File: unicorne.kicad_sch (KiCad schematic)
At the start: 22 parts, among them J1 Battery, J2 TPS43, J3 Expansion, J4 GPIO, J5 PAW3395 / PMW3360, J6 LED power in, Q1 AO3401A, Q2 2N7002, SW43 Power, SW44 Reset, U1 nice!nano v2, U2 SN74LV1T125

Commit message: 0603 resistors and capacitors; rerouted; router rescues stuck signals
- R1-R5, C1, C2 move to KiCad's 0603 hand-solder footprints (README and the
  layout page updated). The last 0805 version is tagged working_0805.
- finish_route.py: when every attempt leaves a signal unrouted, lift one
  neighbouring net in the way, route the connection, reroute the lifted net,
  and keep it only if nothing new is left unrouted. Tracks are removed by
  editing the board file, since removing them through the bindings breaks
  them.
- Both boards: DRC 0 unconnected, schematic parity 0, every pin, the matrix,
  the LED chain and one GND group verified. Gerbers, STEP, renders and plates
  regenerated.

Co-Authored-By: Claude Opus 5.5 <noreply@anthropic.com>
Claude-Session: https://claude.ai/code/session_01D39ubfTYtq6FMvNmmbStTo
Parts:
- C1, C2: footprint Capacitor_SMD:C_0805_2012Metric_Pad1.18x1.45mm_HandSolder -> Capacitor_SMD:C_0603_1608Metric_Pad1.08x0.95mm_HandSolder
- R1, R2, R3, R4, R5: footprint Resistor_SMD:R_0805_2012Metric_Pad1.20x1.40mm_HandSolder -> Resistor_SMD:R_0603_1608Metric_Pad0.98x0.95mm_HandSolder

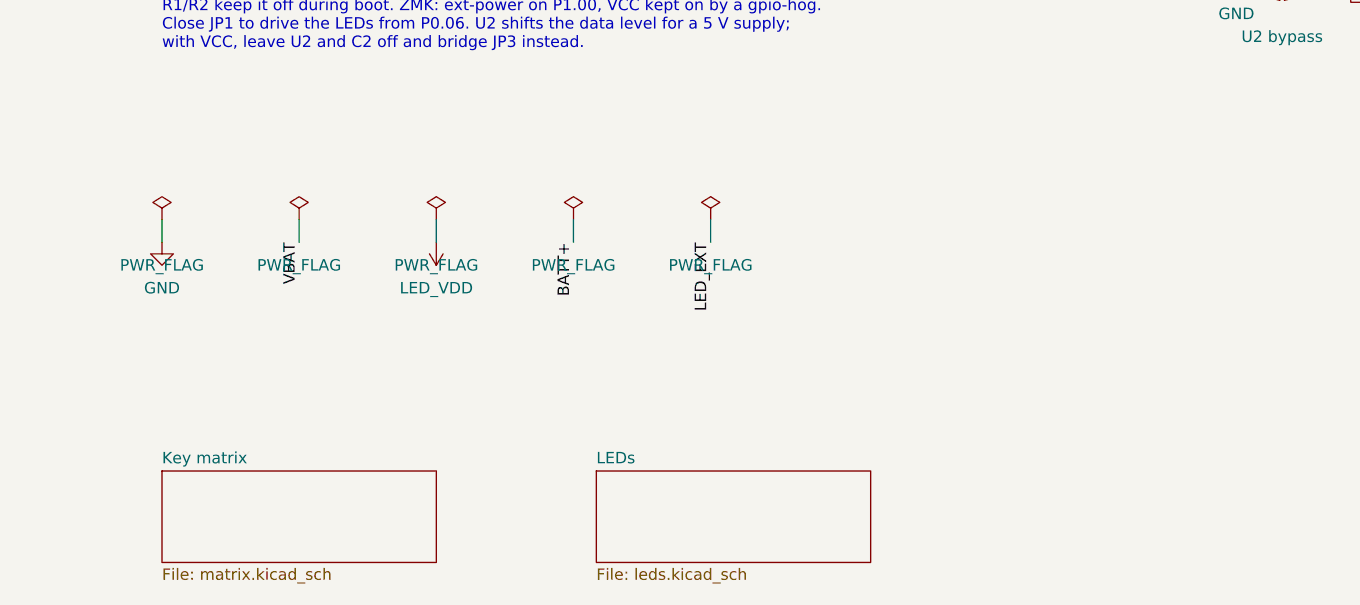
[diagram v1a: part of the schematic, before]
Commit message: Unrouted boards: Pro Micro jumpers, hand-placed centre, new pad rows
Pro Micro mode jumpers JP4-JP6, the hand placement (LED cluster at the
bottom, battery pads by the power switch, reset beside the nice!nano), the
sensor/pull-up/trackpad/UART rows below the nice!nano, and silkscreen that
follows every part. No tracks, vias or zones.

Co-Authored-By: Claude Opus 5.5 <noreply@anthropic.com>
Claude-Session: https://claude.ai/code/session_01D39ubfTYtq6FMvNmmbStTo
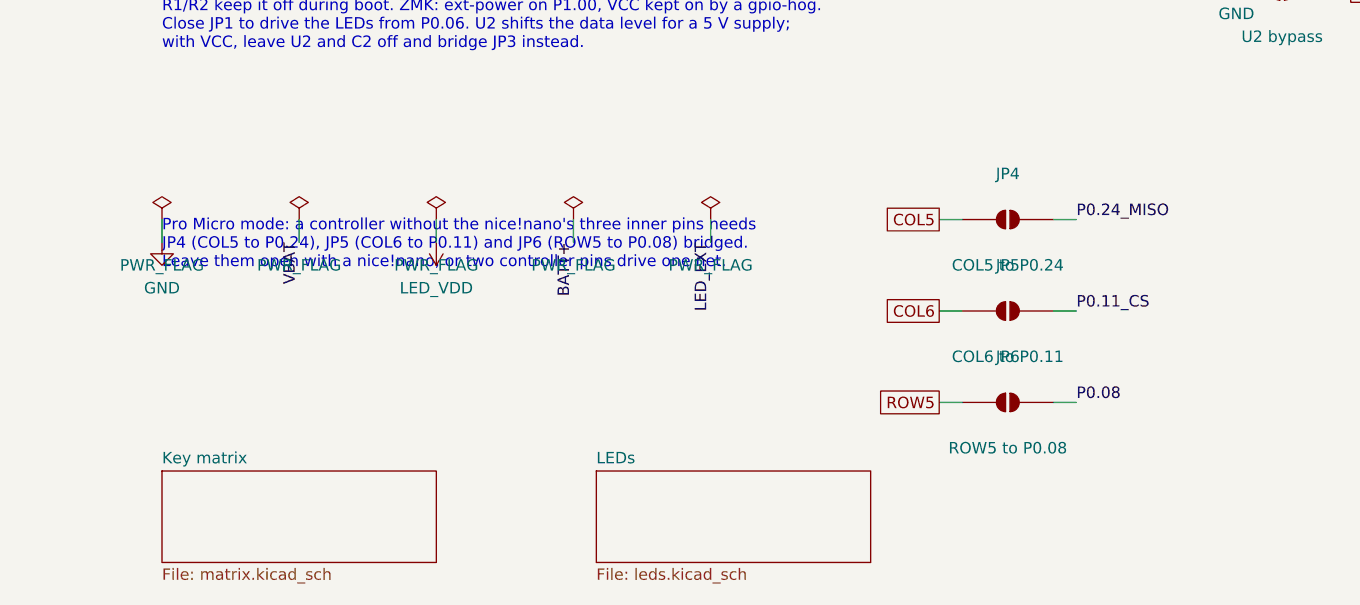
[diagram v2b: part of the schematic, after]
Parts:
- added JP4: COL5 to P0.24, Jumper:SolderJumper-2_P1.3mm_Open_RoundedPad1.0x1.5mm, symbol Jumper:SolderJumper_2_Open
- added JP5: COL6 to P0.11, Jumper:SolderJumper-2_P1.3mm_Open_RoundedPad1.0x1.5mm, symbol Jumper:SolderJumper_2_Open
- added JP6: ROW5 to P0.08, Jumper:SolderJumper-2_P1.3mm_Open_RoundedPad1.0x1.5mm, symbol Jumper:SolderJumper_2_Open
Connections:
- net COL5: now also JP4.1 (A)
- net COL6: now also JP5.1 (A)
- net P0.08: now also JP6.2 (B)
- net P0.11_CS: now also JP5.2 (B)
- net P0.24_MISO: now also JP4.2 (B)
- net ROW5: now also JP6.1 (A)
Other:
- note added: "Pro Micro mode: a controller without the nice!nano's three inner pins needs JP4 (COL5 to P0.24), JP5 (COL6 to P0.11) and JP6 (ROW5 to P0.08) bridged. Leave them open with a nice!nano, or two controller pins drive one net."
